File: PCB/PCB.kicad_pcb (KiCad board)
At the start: 2 copper layers, 186 parts, among them K0,0 KEYSW, K0,1 KEYSW, K0,10 KEYSW, K0,11 KEYSW, K0,12 KEYSW, K0,13 KEYSW, K0,14 KEYSW, K0,15 KEYSW, K0,16 KEYSW, K0,17 KEYSW, K0,18 KEYSW, K0,19 KEYSW, K0,2 KEYSW, K0,20 KEYSW, K0,3 KEYSW, K0,4 KEYSW, K0,5 KEYSW, K0,6 KEYSW, K0,7 KEYSW, K0,8 KEYSW, K0,9 KEYSW, K1,0 KEYSW, K1,1 KEYSW, K1,10 KEYSW, K1,11 KEYSW, K1,12 KEYSW, K1,13 KEYSW, K1,14 KEYSW, K1,15 KEYSW, K1,16 KEYSW, K1,17 KEYSW, K1,18 KEYSW, K1,19 KEYSW, K1,2 KEYSW, K1,20 KEYSW, K1,3 KEYSW, K1,4 KEYSW, K1,5 KEYSW, K1,6 KEYSW, K1,7 KEYSW, K1,8 KEYSW, K1,9 KEYSW, K2,0 KEYSW, K2,1 KEYSW, K2,10 KEYSW, K2,11 KEYSW, K2,12 KEYSW, K2,13 KEYSW, K2,14 KEYSW, K2,15 KEYSW, K2,17 KEYSW, K2,18 KEYSW, K2,19 KEYSW, K2,2 KEYSW, K2,20 KEYSW, K2,4 KEYSW, K2,5 KEYSW, K2,6 KEYSW, K2,7 KEYSW, K2,8 KEYSW, K2,9 KEYSW, K3,0 KEYSW, K3,1 KEYSW, K3,10 KEYSW, K3,11 KEYSW, K3,12 KEYSW, K3,13 KEYSW, K3,14 KEYSW, K3,17 KEYSW, K3,18 KEYSW, K3,19 KEYSW, K3,2 KEYSW, K3,20 KEYSW, K3,3 KEYSW, K3,4 KEYSW, K3,5 KEYSW, K3,6 KEYSW, K3,7 KEYSW, K3,8 KEYSW, K3,9 KEYSW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

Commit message: Oriented diodes; laid down MCU and BT module
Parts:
- removed D3,17: D, keyboard_parts:D_SOD123_axial
- removed K3,17: KEYSW, keebs:Mx_Alps_275
- added D3,16: D, keyboard_parts:D_SOD123_axial, B.Cu at (428.6, 221.5)
- added K3,16: KEYSW, keebs:Mx_Alps_275, F.Cu at (428.6, 216.7)
- D0,0, D0,1, D0,10, D0,11, D0,12, D0,13, D0,14, D0,15, D0,16, D0,17, D0,18, D0,19, D0,2, D0,20, D0,3, D0,4, D0,5, D0,6, D0,7, D0,8, D0,9, D1,0, D1,1, D1,10, D1,11, D1,12, D1,13, D1,14, D1,15, D1,16, D1,17, D1,18, D1,19, D1,2, D1,20, D1,3, D1,4, D1,5, D1,6, D1,7, D1,8, D1,9, D2,0, D2,1, D2,10, D2,11, D2,12, D2,13, D2,14, D2,15, D2,17, D2,18, D2,19, D2,2, D2,20, D2,4, D2,5, D2,6, D2,7, D2,8, D2,9, D3,0, D3,1, D3,10, D3,11, D3,12, D3,13, D3,14, D3,18, D3,19, D3,2, D3,20, D3,3, D3,4, D3,5, D3,6, D3,7, D3,8, D3,9, D4,0, D4,13, D4,14, D4,16, D4,17, D4,18, D4,19, D4,2, D4,20, D4,4, D4,5, D4,6, D4,9: moved to B.Cu
- moved D4,20 240.5 mm to (502.4, 240.5)
- moved D3,20 236.4 mm to (502.4, 221.5)
- moved D2,20 233.7 mm to (502.4, 202.4)
- moved D0,20 233.0 mm to (502.4, 164.3)
- moved D1,20 232.5 mm to (502.4, 183.4)
- moved D4,19 222.2 mm to (483.4, 240.5)
- moved D3,19 217.7 mm to (483.4, 221.5)
- moved D2,19 214.7 mm to (483.4, 202.4)
- moved D0,19 213.9 mm to (483.4, 164.3)
- moved D1,19 213.5 mm to (483.4, 183.4)
- moved D4,18 204.0 mm to (464.3, 240.5)
- moved D3,18 199.0 mm to (464.3, 221.5)
- moved D2,18 195.8 mm to (464.3, 202.4)
- moved D0,18 194.9 mm to (464.3, 164.3)
- moved D1,18 194.5 mm to (464.3, 183.4)
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
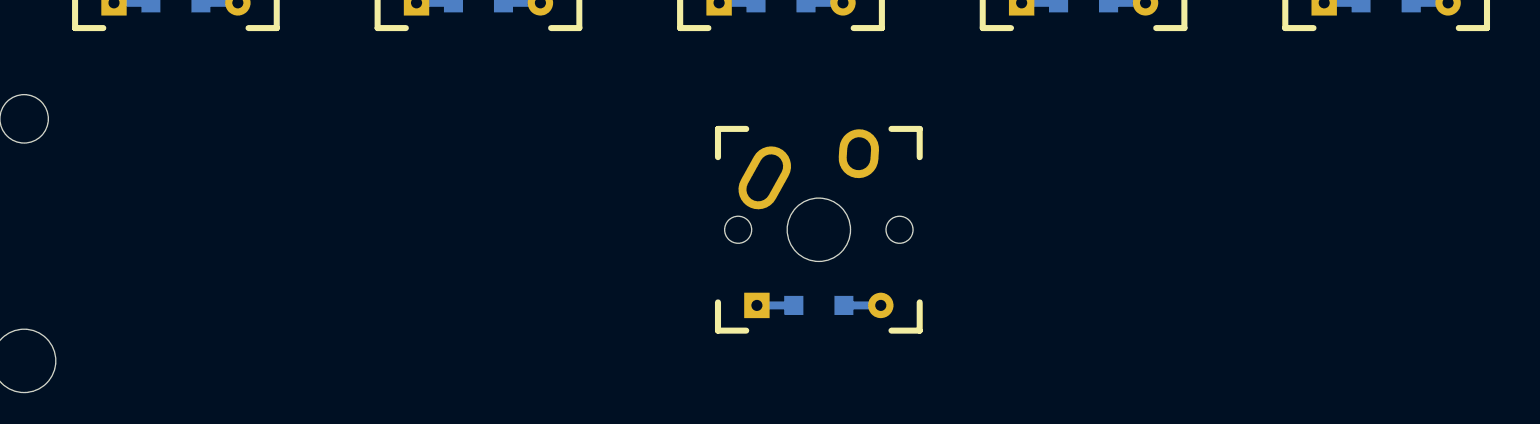
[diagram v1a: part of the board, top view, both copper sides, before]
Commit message: Switched MCUs; removed BT for now
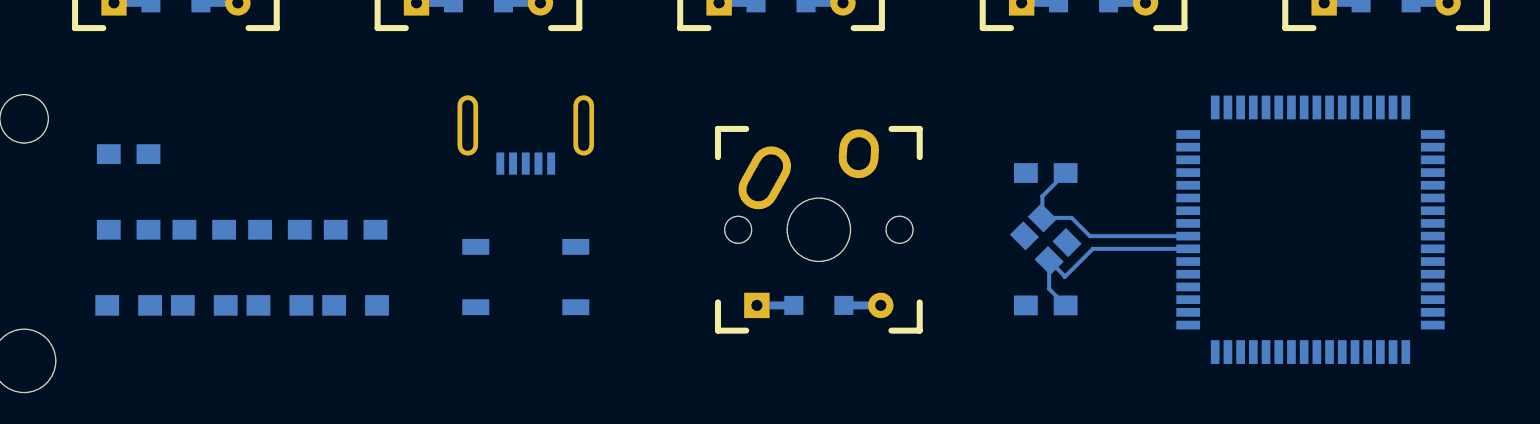
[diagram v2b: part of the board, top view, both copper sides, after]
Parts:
- added C1: 22p, Capacitors_SMD:C_0805_HandSoldering, B.Cu at (314.3, 232.2)
- added C2: 22p, Capacitors_SMD:C_0805_HandSoldering, B.Cu at (314.3, 240.5)
- added C3: 0.1u, Capacitors_SMD:C_0805_HandSoldering, B.Cu at (256.6, 235.7)
- added C4: 0.1u, Capacitors_SMD:C_0805_HandSoldering, B.Cu at (261.3, 235.7)
- added C5: 0.1u, Capacitors_SMD:C_0805_HandSoldering, B.Cu at (266.1, 235.7)
- added C7: 4.7u, Capacitors_SMD:C_0805_HandSoldering, B.Cu at (270.9, 235.7)
- added CU1: 1u, Capacitors_SMD:C_0805_HandSoldering, B.Cu at (256.6, 231.0)
- added J1: USB_mini_micro_B, keyboard_parts:USB_miniB_hirose_5S8, B.Cu at (281.6, 231.6)
- added RR1: 10k, Resistors_SMD:R_0805_HandSoldering, B.Cu at (266.1, 240.5)
- added RR2: 10k, Resistors_SMD:R_0805_HandSoldering, B.Cu at (270.9, 240.5)
- added RU1: 22, Resistors_SMD:R_0805_HandSoldering, B.Cu at (256.6, 240.5)
- added RU2: 22, Resistors_SMD:R_0805_HandSoldering, B.Cu at (261.3, 240.5)
- added SW1: SW_PUSH, Buttons_Switches_SMD:SW_SPST_TL3342, B.Cu at (281.6, 238.7)
- added U1: AT90USB1286, Housings_QFP:TQFP-64_14x14mm_Pitch0.8mm, B.Cu at (331.0, 235.7)
- added X1: XTAL_GND, Crystals:crystal_FA238-TSX3225, B.Cu at (314.3, 236.3)
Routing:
- net Net-(C2-Pad1): track 0.00 -> 13.2 mm
- net Net-(C1-Pad1): track 0.00 -> 13.1 mm

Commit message: USB routed and most components connected
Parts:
- removed C7: 4.7u, Capacitors_SMD:C_0805_HandSoldering
- added C6: 4.7u, Capacitors_SMD:C_0805_HandSoldering, B.Cu at (311.3, 234.0)
- moved RU2 89.5 mm to (303.0, 161.3), turned to 90 degrees
- moved C3 84.7 mm to (341.1, 230.4)
- moved J1 78.4 mm to (302.4, 156.0)
- moved RU1 71.8 mm to (292.9, 178.6), turned to 90 degrees
- moved RR2 70.2 mm to (341.1, 241.1), turned to 180 degrees
- moved CU1 54.8 mm to (311.3, 230.4), turned to 180 degrees
- moved C4 50.3 mm to (311.3, 241.1), turned to 180 degrees
- moved C5 45.3 mm to (311.3, 237.5), turned to 180 degrees
- moved C2 27.6 mm to (341.1, 234.0), turned to 0 degrees
- moved C1 27.3 mm to (341.1, 237.5), turned to 0 degrees
- moved X1 22.6 mm to (334.6, 226.2), turned to 180 degrees
- moved RR1 20.2 mm to (285.8, 235.7), turned to 90 degrees
- moved SW1 6.13 mm to (276.2, 235.7), turned to 270 degrees
- moved U1 4.76 mm to (326.2, 235.7), turned to 315 degrees
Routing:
- net VCC: track 0.00 -> 169.6 mm
- net Net-(RU2-Pad1): track 0.00 -> 85.6 mm, vias 0 -> 2
- net Net-(RU1-Pad1): track 0.00 -> 65.4 mm, vias 0 -> 2
- net Net-(J1-Pad2): track 0.00 -> 24.9 mm
- net Net-(RR2-Pad2): track 0.00 -> 10.8 mm
- net Net-(CU1-Pad1): track 0.00 -> 8.15 mm
- net Net-(C2-Pad1): track 13.2 -> 20.0 mm
- net Net-(C1-Pad1): track 13.1 -> 17.7 mm
- net Net-(J1-Pad3): track 0.00 -> 4.25 mm
- net GND: track 0.00 -> 2.82 mm
- added copper zone on B.Cu, net GND
- added copper zone on F.Cu, net GND
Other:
- board outline added: 419.1 x 97.6 mm

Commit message: Connected columns and rows
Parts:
- turned SW1 to 0 degrees
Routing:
- net /row0: track 0.00 -> 439.7 mm, vias 0 -> 2
- net /row1: track 0.00 -> 439.2 mm, vias 0 -> 2
- net /row2: track 0.00 -> 435.8 mm, vias 0 -> 2
- net /row3: track 0.00 -> 435.3 mm, vias 0 -> 2
- net /row4: track 0.00 -> 414.3 mm, vias 0 -> 2
- net /col5: track 0.00 -> 101.2 mm
- net /col6: track 0.00 -> 97.8 mm
- net /col9: track 0.00 -> 95.5 mm
- net /col14: track 0.00 -> 95.5 mm
- net /col13: track 0.00 -> 93.8 mm
- net /col16: track 0.00 -> 93.2 mm
- net /col4: track 0.00 -> 89.9 mm
- net /col17: track 0.00 -> 88.3 mm
- net /col0: track 0.00 -> 87.6 mm
- net /col3: track 0.00 -> 87.2 mm
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
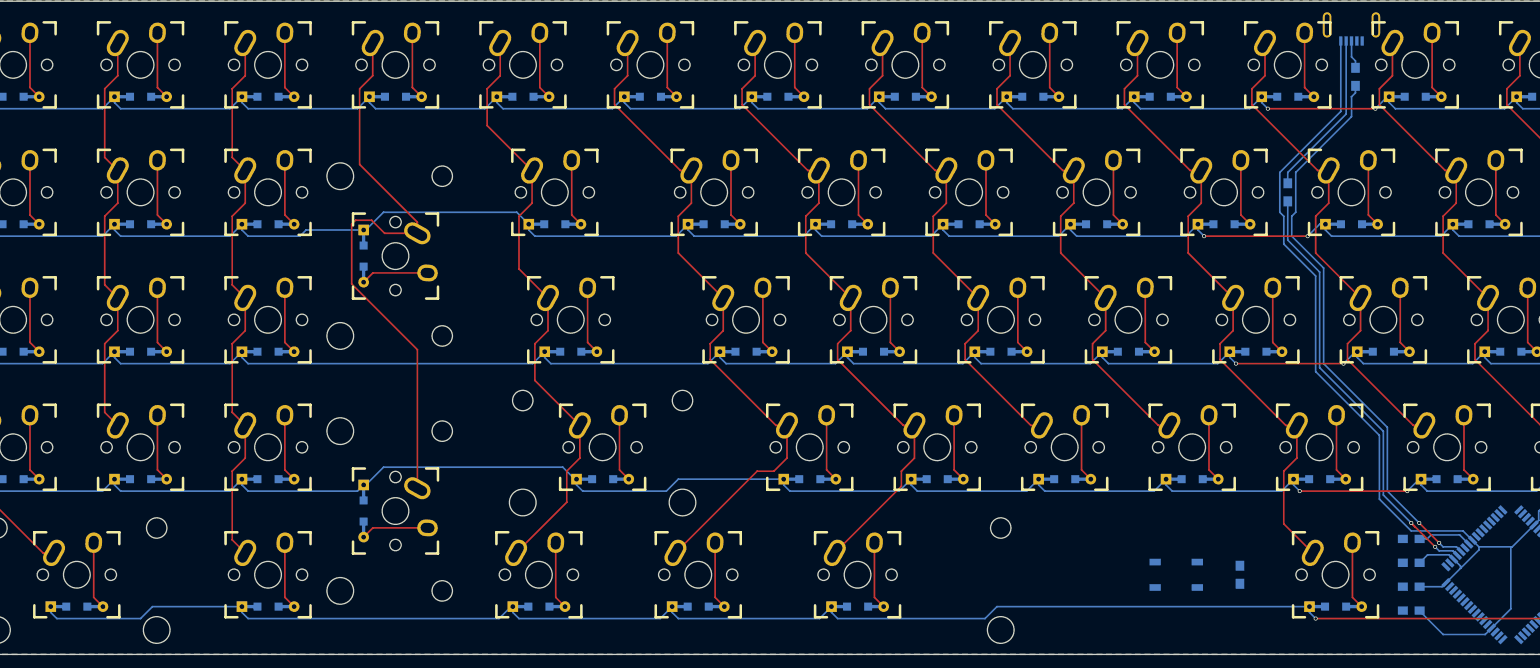
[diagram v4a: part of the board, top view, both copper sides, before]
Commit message: Additional routing: col1 and col2 connected
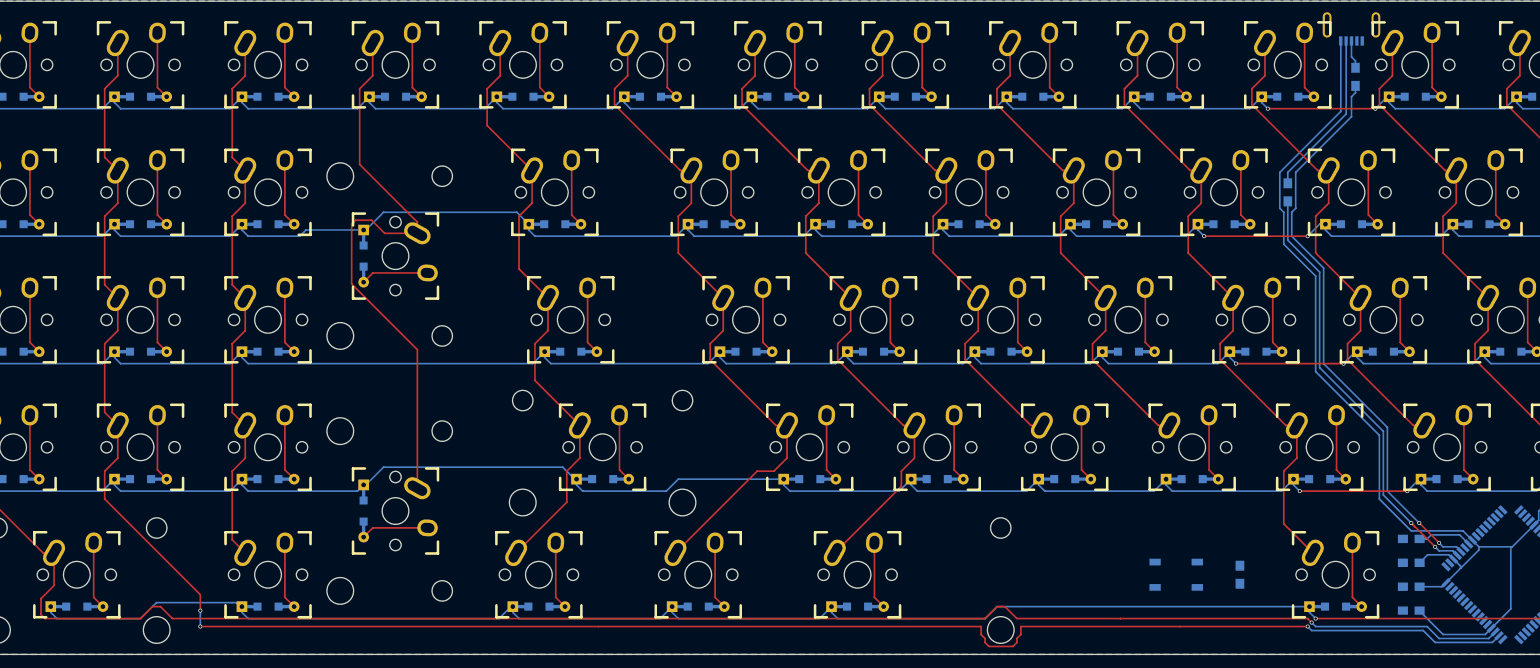
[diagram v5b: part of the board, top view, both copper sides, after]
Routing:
- net /col1: track 62.0 -> 298.8 mm, vias 0 -> 3
- net /col0: track 87.6 -> 319.8 mm, vias 0 -> 1
- net VCC: track 169.6 -> 169.1 mm

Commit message: Trying a new MCU orientation to make room routes
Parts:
- moved RR1 56.3 mm to (341.1, 225.6), turned to 0 degrees
- moved C3 38.6 mm to (309.0, 251.8)
- moved RR2 36.8 mm to (309.0, 259.0)
- moved C4 32.5 mm to (341.1, 228.0), turned to 0 degrees
- moved X1 25.7 mm to (340.5, 251.2), turned to 315 degrees
- moved SW1 24.3 mm to (290.5, 255.4)
- moved CU1 8.42 mm to (310.2, 238.7)
- moved C6 7.24 mm to (310.2, 241.1)
- moved C1 4.76 mm to (341.1, 232.8)
- moved C2 3.57 mm to (341.1, 230.4)
- moved C5 1.68 mm to (310.2, 236.3)
- turned U1 to 0 degrees
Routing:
- net /col1: track 298.8 -> 62.0 mm, vias 3 -> 0
- net /col0: track 319.8 -> 87.6 mm, vias 1 -> 0
- net /col15: track 48.2 -> 162.8 mm, vias 0 -> 1
- net /col14: track 95.5 -> 176.2 mm, vias 0 -> 1
- net /col8: track 73.8 -> 136.1 mm, vias 0 -> 3
- net /col13: track 93.8 -> 153.5 mm, vias 0 -> 1
- net /col12: track 73.8 -> 123.0 mm, vias 0 -> 1
- net /col11: track 73.8 -> 106.2 mm, vias 0 -> 1
- net /col9: track 95.5 -> 124.0 mm, vias 0 -> 1
- net /col10: track 73.8 -> 98.4 mm, vias 0 -> 1
- net Net-(RR1-Pad1): track 0.00 -> 20.0 mm
- net Net-(RR2-Pad2): track 10.8 -> 0.00 mm
- net VCC: track 169.1 -> 162.6 mm
- net Net-(RU2-Pad1): track 85.2 -> 91.0 mm
- net Net-(RU1-Pad1): track 65.4 -> 71.1 mm
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
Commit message: Reached a roadblock with this orientation
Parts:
- moved SW1 55.0 mm to (343.5, 240.5), turned to 90 degrees
- moved C3 40.0 mm to (341.1, 228.0)
- moved RR2 40.0 mm to (341.1, 235.1)
- moved C4 21.8 mm to (328.6, 245.9), turned to 180 degrees
- moved X1 20.7 mm to (326.8, 235.7)
- moved C5 5.36 mm to (310.2, 241.7)
- moved CU1 1.79 mm to (310.2, 236.9)
- moved C6 1.79 mm to (310.2, 239.3)
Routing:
- net /row1: track 439.2 -> 535.5 mm, vias 2 -> 4
- net /row2: track 435.8 -> 513.4 mm, vias 2 -> 4
- net /row3: track 435.3 -> 499.8 mm, vias 2 -> 4
- net /row4: track 414.8 -> 458.1 mm
- net Net-(RR1-Pad1): track 20.0 -> 45.4 mm, vias 0 -> 2
- net Net-(RR2-Pad2): track 0.00 -> 8.05 mm
- net VCC: track 162.6 -> 168.1 mm
- net /col11: track 106.2 -> 103.4 mm
- net Net-(CU1-Pad1): track 7.87 -> 8.61 mm

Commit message: Rotated MCU; rerouting
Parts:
- moved CU1 33.1 mm to (342.9, 232.2), turned to 0 degrees
- moved RR2 31.8 mm to (309.6, 239.3), turned to 0 degrees
- moved C4 21.0 mm to (309.6, 236.9)
- moved RR1 18.3 mm to (359.0, 229.8), turned to 180 degrees
- moved SW1 16.2 mm to (359.0, 235.7), turned to 270 degrees
- moved X1 10.1 mm to (336.9, 235.1), turned to 135 degrees
- moved C5 7.17 mm to (309.6, 234.6)
- moved C6 7.17 mm to (309.6, 232.2)
- moved C1 6.79 mm to (342.9, 239.3)
- moved C3 6.79 mm to (342.9, 234.6)
- moved C2 6.79 mm to (342.9, 236.9)
- moved U1 1.19 mm to (325.0, 235.7), turned to 270 degrees
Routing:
- net /col15: track 162.8 -> 50.7 mm
- net /row1: track 535.5 -> 441.7 mm, vias 4 -> 3
- net /col14: track 176.2 -> 100.9 mm
- net /row2: track 513.4 -> 438.3 mm, vias 4 -> 3
- net /row3: track 499.8 -> 437.9 mm, vias 4 -> 3
- net /col8: track 136.1 -> 77.9 mm, vias 3 -> 1
- net /col13: track 153.5 -> 97.9 mm
- net /col12: track 123.0 -> 77.6 mm
- net /row4: track 458.1 -> 419.8 mm, vias 2 -> 3
- net Net-(RR1-Pad1): track 45.4 -> 9.33 mm, vias 2 -> 0
- net GND: track 0.00 -> 31.7 mm
- net /col11: track 103.4 -> 77.9 mm
- net /col9: track 124.0 -> 99.5 mm
- net /col10: track 98.4 -> 77.6 mm
- net Net-(CU1-Pad1): track 8.61 -> 21.8 mm
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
